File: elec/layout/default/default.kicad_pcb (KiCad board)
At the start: 4 copper layers, 76 x 142 mm, 113 parts, among them J1 ?, J2 ?, J3 ?, Q1 ?, Q2 ?, SW1 ?, SW10 ?, SW11 ?, SW12 ?, SW13 ?, SW14 ?, SW15 ?, SW16 ?, SW17 ?, SW18 ?, SW19 ?, SW2 ?, SW20 ?, SW21 ?, SW22 ?, SW23 ?, SW24 ?, SW25 ?, SW26 ?, SW27 ?, SW28 ?, SW29 ?, SW3 ?, SW30 ?, SW31 ?, SW32 ?, SW33 ?, SW34 ?, SW35 ?, SW36 ?, SW37 ?, SW38 ?, SW39 ?, SW4 ?, SW40 ?, SW5 ?, SW6 ?, SW7 ?, SW8 ?, SW9 ?, U1 ?, U10 ?, U2 ?, U3 ?, U4 ?, U5 ?, U6 ?, U7 ?, U8 ?, U9 ?

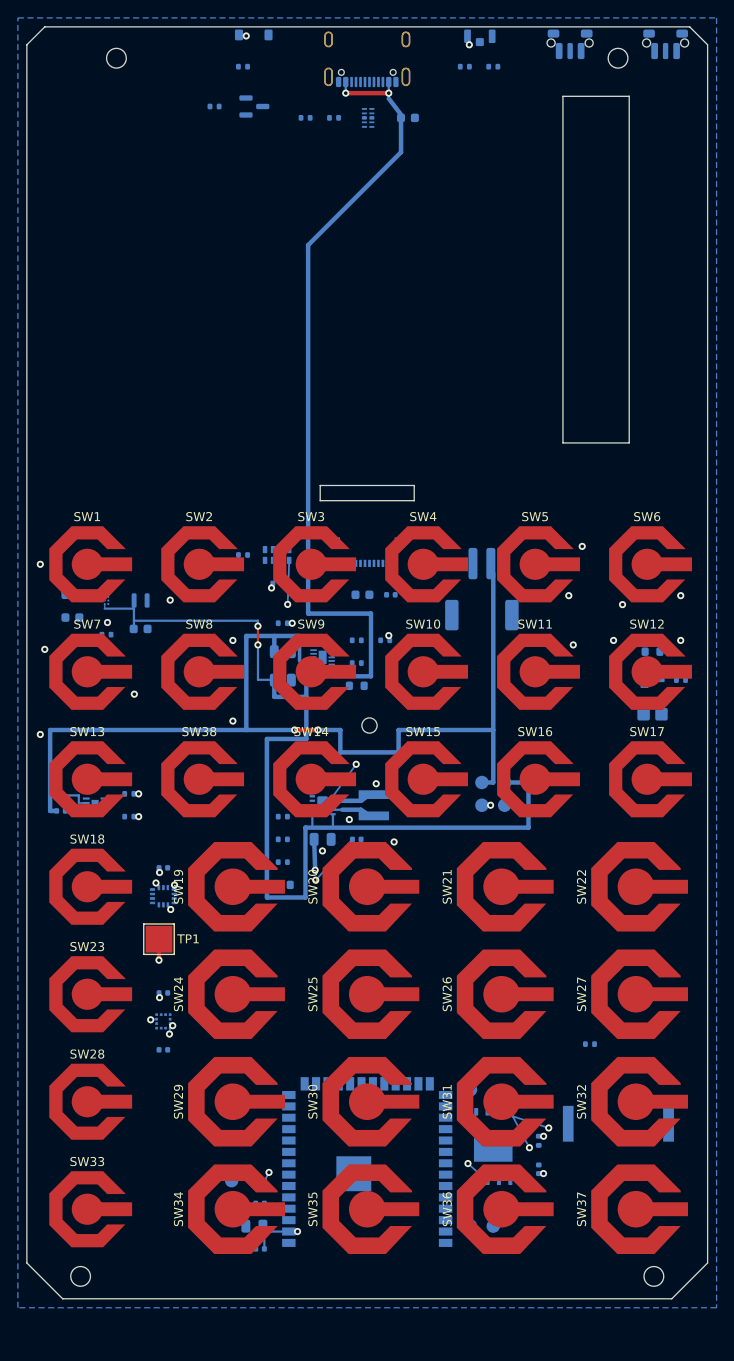
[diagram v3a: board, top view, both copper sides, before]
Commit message: ls027: signals routed and straightened, 2.7in panel and 6x38x50 cell models, ST sensor bodies
route_signals: 120 nets, 0 failed, audit clean. straighten.py: 2195 -> 1271
segments, same per-net connectivity. check_ends and check_pour clean.

Co-Authored-By: Claude Opus 5.5 (1M context) <noreply@anthropic.com>
Claude-Session: https://claude.ai/code/session_01Fsrot3PauY1JdFC7HgzJ33
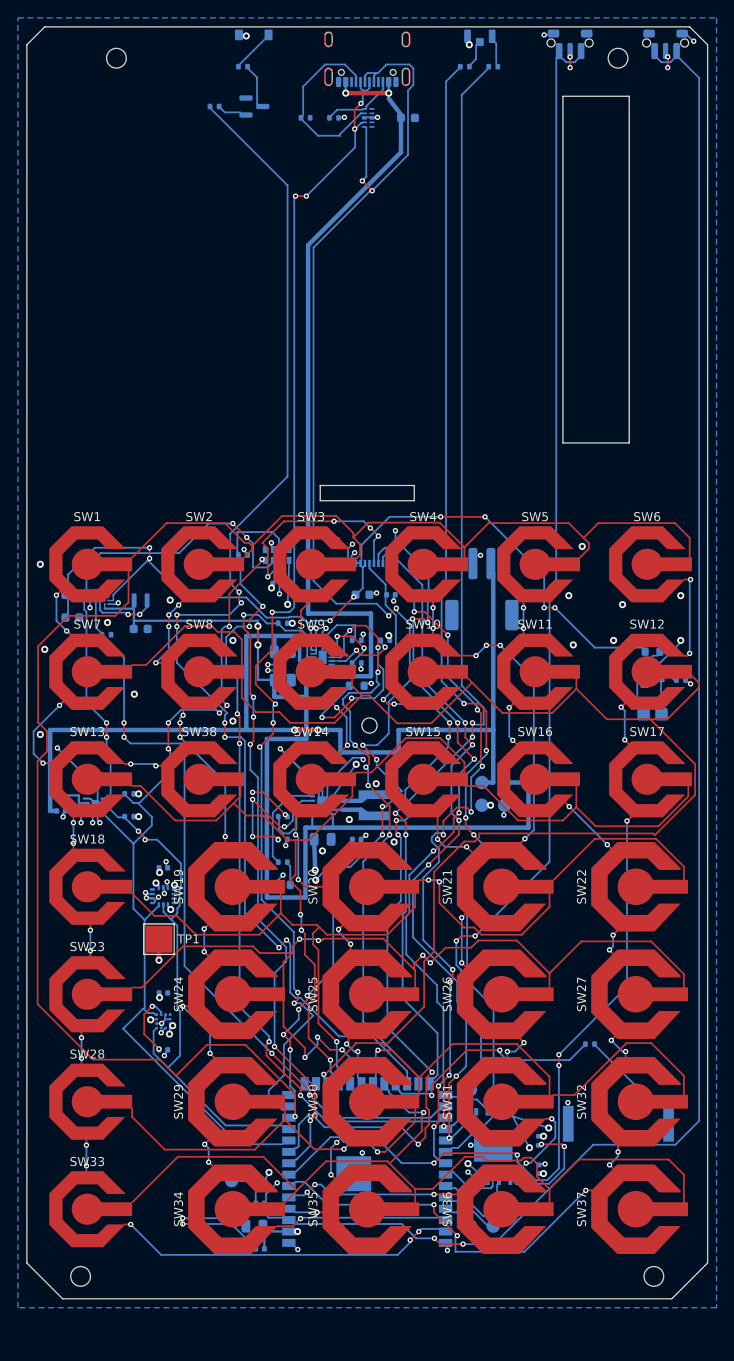
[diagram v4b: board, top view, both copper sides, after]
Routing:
- net en: track 0.00 -> 180.5 mm, vias 0 -> 2
- net row0: track 0.00 -> 178.0 mm, vias 0 -> 1
- net row1: track 0.00 -> 161.6 mm, vias 0 -> 1
- net usb_dp: track 0.00 -> 154.6 mm, vias 0 -> 12
- net led_red: track 0.00 -> 149.6 mm, vias 0 -> 6
- net ir_led: track 0.00 -> 137.3 mm, vias 0 -> 8
- net led_green: track 0.00 -> 130.9 mm, vias 0 -> 4
- net usb_dm: track 0.00 -> 130.8 mm, vias 0 -> 10
- net boot: track 0.00 -> 125.6 mm, vias 0 -> 2
- net row2: track 0.00 -> 112.1 mm, vias 0 -> 3
- net i2c_scl: track 0.00 -> 111.6 mm, vias 0 -> 6
- net gnd: track 1.40 -> 111.8 mm, vias 20 -> 80
- net row4: track 0.00 -> 100.1 mm, vias 0 -> 7
- net row3: track 0.00 -> 99.6 mm, vias 0 -> 3
- net i2c_sda: track 0.00 -> 98.6 mm, vias 0 -> 6
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
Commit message: ls027: FPC connector for the Azumo LED flex, taller status LED, six board-to-front-shell holes
J3 is now a 2-way 1.0 mm top-contact ZIF (C53145530) on the flex end.
D2 is the XL-C4040 (lens 2.0 up), driven back to back on IO16/IO39.
Holes E/F (M2), H/I and J/K (M1.6), mirrored about X 38; L2, C11, the
buzzer and the boost's sys feed moved for them. Pad nets synced with the
netlist (IO3 and IO46 now reach the IMU and the front light switch).
Touched nets rerouted and straightened; all-copper clearance check clean.

Co-Authored-By: Claude Opus 5.5 (1M context) <noreply@anthropic.com>
Claude-Session: https://claude.ai/code/session_01Fsrot3PauY1JdFC7HgzJ33
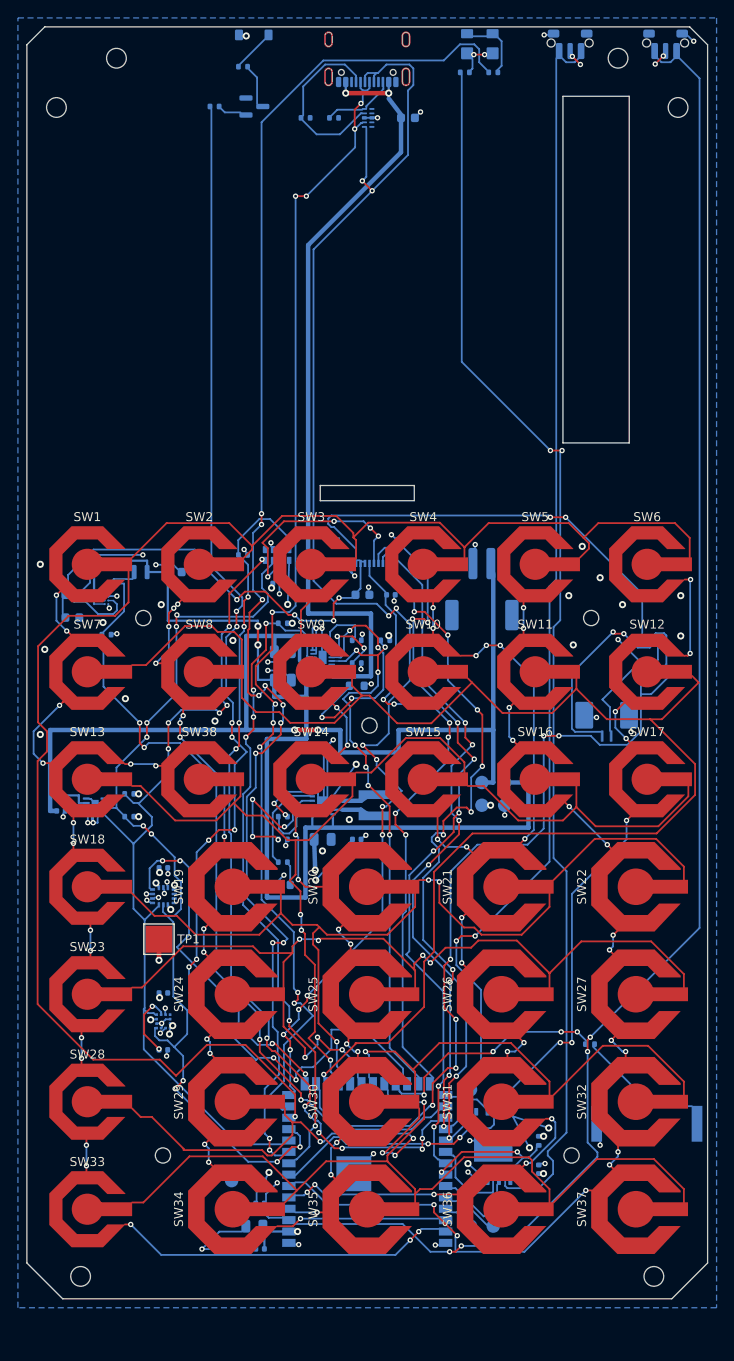
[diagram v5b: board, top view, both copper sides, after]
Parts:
- D2: footprint hp42s:LiteOn_LTST-S326_BiColor_RA -> hp42s:XINGLIGHT_XL-C4040_SideView
- J3: footprint hp42s:Azumo_FLP_LED_WirePads -> hp42s:FPC_1.0mm_2P_TopContact_1.0K-LS
- moved C11 7.41 mm to (16.5, 60.9)
- moved J3 5.13 mm to (64.7, 76.7), turned to 180 degrees
- moved L2 3.18 mm to (12.7, 60.9), turned to 180 degrees
- moved LS1 3.17 mm to (69.2, 122.5)
- moved Q2 1.27 mm to (69.8, 71.7)
- moved R24 1.27 mm to (73.0, 71.7)
- moved R23 1.27 mm to (69.8, 68.5)
- moved D2 0.72 mm to (50.6, 1.77)
- moved R20 0.63 mm to (52.1, 5.08)
- moved R21 0.63 mm to (48.9, 5.08)
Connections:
- net int renamed display.rtc-int
- D2 pad 1: ygreen -> t_red
- D2 pad 2: v3v3 -> t_green
- D2 pad 3: red -> t_red
- R20 pad 2: red -> t_red
- R21 pad 2: ygreen -> t_green
- U5 pad 15: io3 -> imu_int1
- U5 pad 16: io46 -> fl_en
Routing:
- net fl_en: track 3.76 -> 90.5 mm, vias 0 -> 6
- net imu_int1: track 0.00 -> 38.6 mm, vias 0 -> 4
- net fl_k: track 3.11 -> 27.7 mm, vias 0 -> 2
- net led_green: track 130.9 -> 148.3 mm, vias 4 -> 2
- net sys: track 112.4 -> 123.1 mm
- net col5: track 92.2 -> 82.0 mm
- net led_red: track 149.6 -> 159.6 mm, vias 6 -> 12
- net row5: track 92.7 -> 102.5 mm, vias 3 -> 5
- net v5: track 95.3 -> 104.3 mm, vias 8 -> 6
- net gnd: track 111.8 -> 103.2 mm, vias 80 -> 78
- net i2c_scl: track 111.6 -> 103.6 mm, vias 6 -> 10
- net fl_a: track 7.14 -> 13.6 mm
- net mip_pwr: track 85.0 -> 91.2 mm
- net flash_cs: track 21.2 -> 15.2 mm
- net mip_clkoe: track 92.2 -> 97.8 mm, vias 6 -> 10
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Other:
- outline, holes or cut-outs redrawn

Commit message: ls027: top-band parts moved up out of the cell's way, 6x40x50 (604050) bay, Azumo STEP as the panel model
Q1/R18/R19 up beside D1, C1 right of J1, U1 turned 90 so U1/R1/R2 make
one row under J1. Bay X 5.5..55.5, Y 10.5..50.5; battery_life 1300 mAh.
VBUS J1->C1 along Y 7.75, down from C1 at x 45.58. usb/cc/IR nets and gnd
tails rerouted, straightened; ends, pour and clearance checked.
mech_models builds Mech_Panel from Azumo's FLP 11103-06 STEP (vendor-3d),
panel FPC cut at Y 50.92 and folded into J2.

Co-Authored-By: Claude Opus 5.5 (1M context) <noreply@anthropic.com>
Claude-Session: https://claude.ai/code/session_01Fsrot3PauY1JdFC7HgzJ33
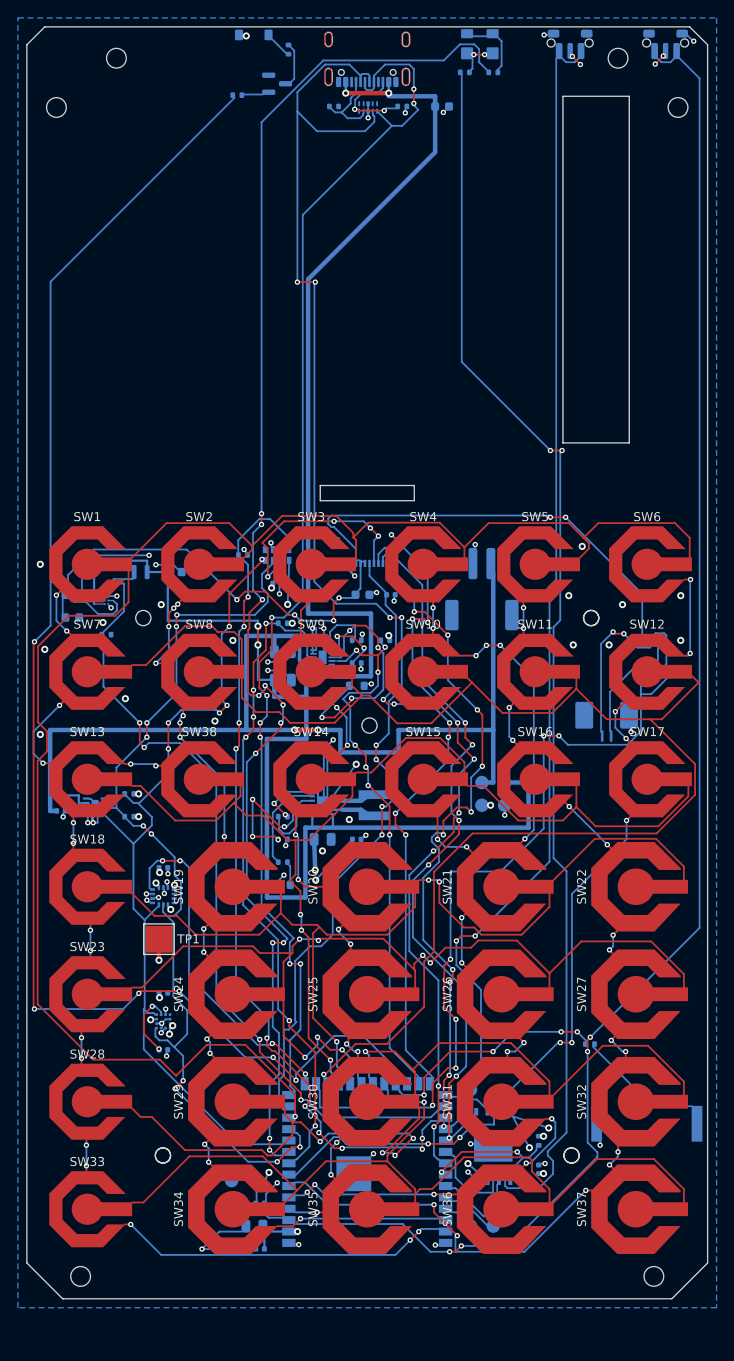
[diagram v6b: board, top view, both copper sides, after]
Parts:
- moved R2 7.73 mm to (41.9, 8.89)
- moved R18 5.43 mm to (29.2, 2.54), turned to 90 degrees
- moved C1 4.02 mm to (46.4, 8.89)
- moved Q1 3.59 mm to (27.9, 6.35)
- moved R1 3.42 mm to (34.3, 8.89)
- moved R19 2.84 mm to (23.5, 7.62)
- moved U1 1.16 mm to (38.1, 9.00), turned to 90 degrees
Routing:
- net usb_dm: track 130.8 -> 152.4 mm, vias 10 -> 8
- net ir_led: track 140.5 -> 161.8 mm, vias 10 -> 6
- net usb_dp: track 153.2 -> 136.5 mm, vias 12 -> 8
- net cc1: track 19.1 -> 7.84 mm
- net vbus: track 89.0 -> 95.6 mm
- net fl_k: track 27.7 -> 23.3 mm
- net gnd: track 103.2 -> 99.4 mm, vias 78 -> 76
- net cc2: track 6.91 -> 10.0 mm, vias 0 -> 2
- net cathode: track 3.89 -> 2.12 mm
- net fl_en: track 90.5 -> 88.8 mm
- net mip_pwr: track 91.2 -> 89.7 mm
- net imu_int1: track 38.6 -> 37.5 mm
- net led_red: track 159.6 -> 158.7 mm
- net mip_clkoe: track 97.8 -> 97.0 mm
- net mip_cs: track 84.1 -> 83.3 mm
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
